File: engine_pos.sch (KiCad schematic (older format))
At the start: 12 parts, among them U5 MAX9926

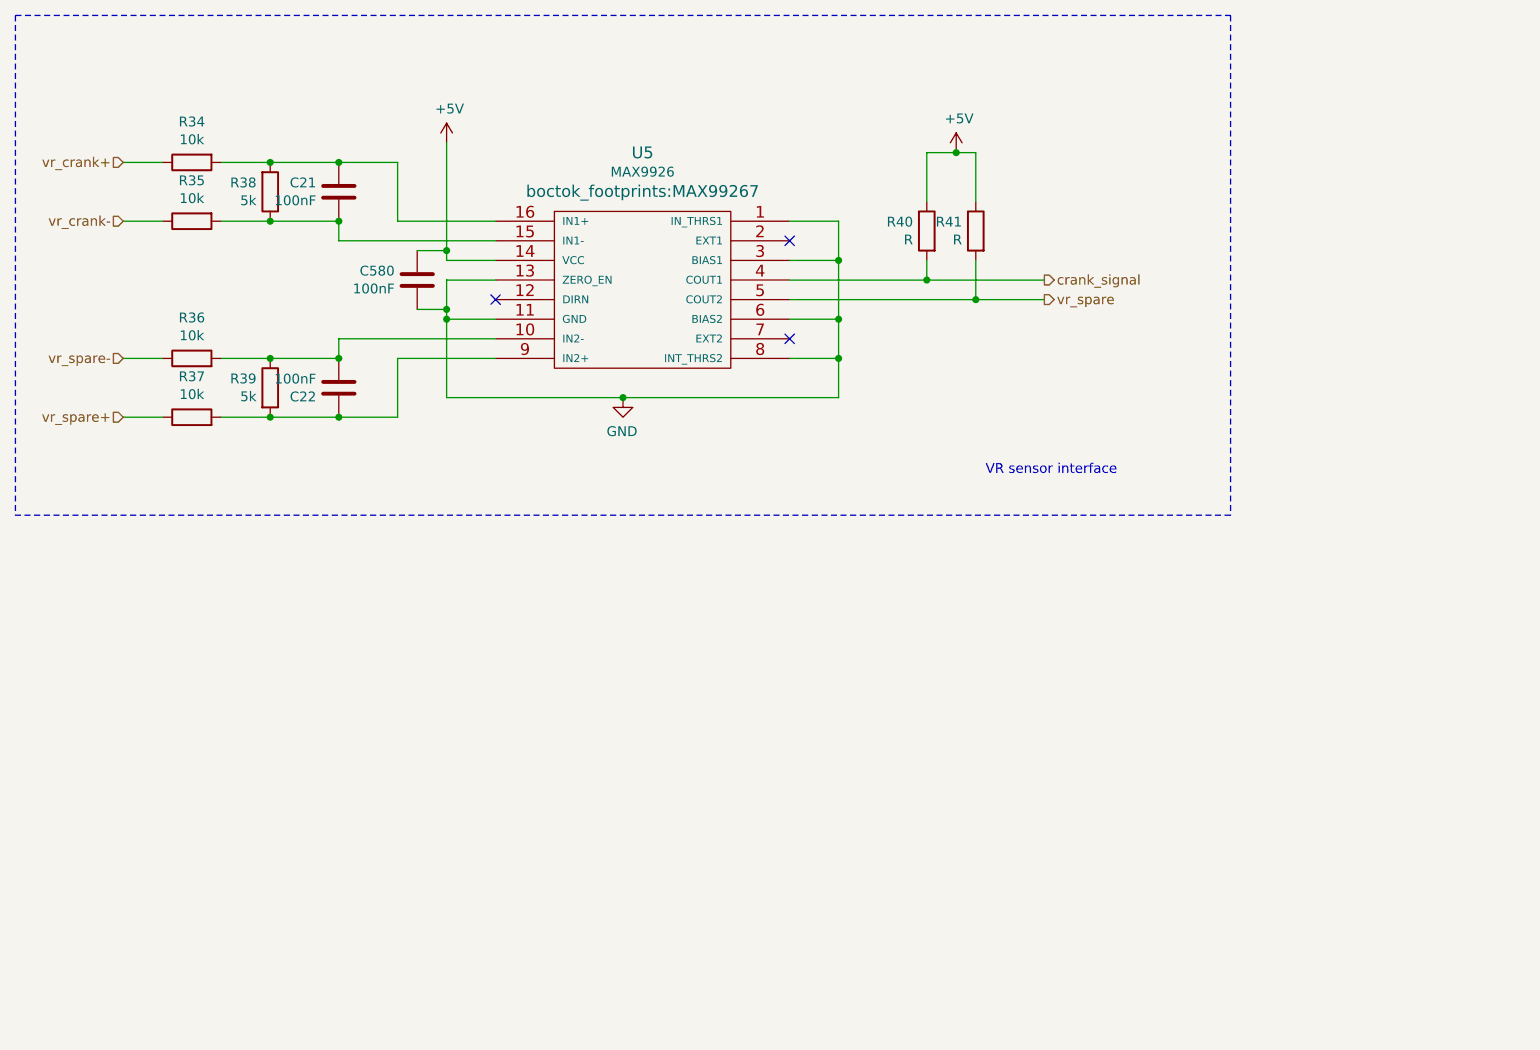
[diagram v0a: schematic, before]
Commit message: changed to discrete crank vr sensor cirquitry
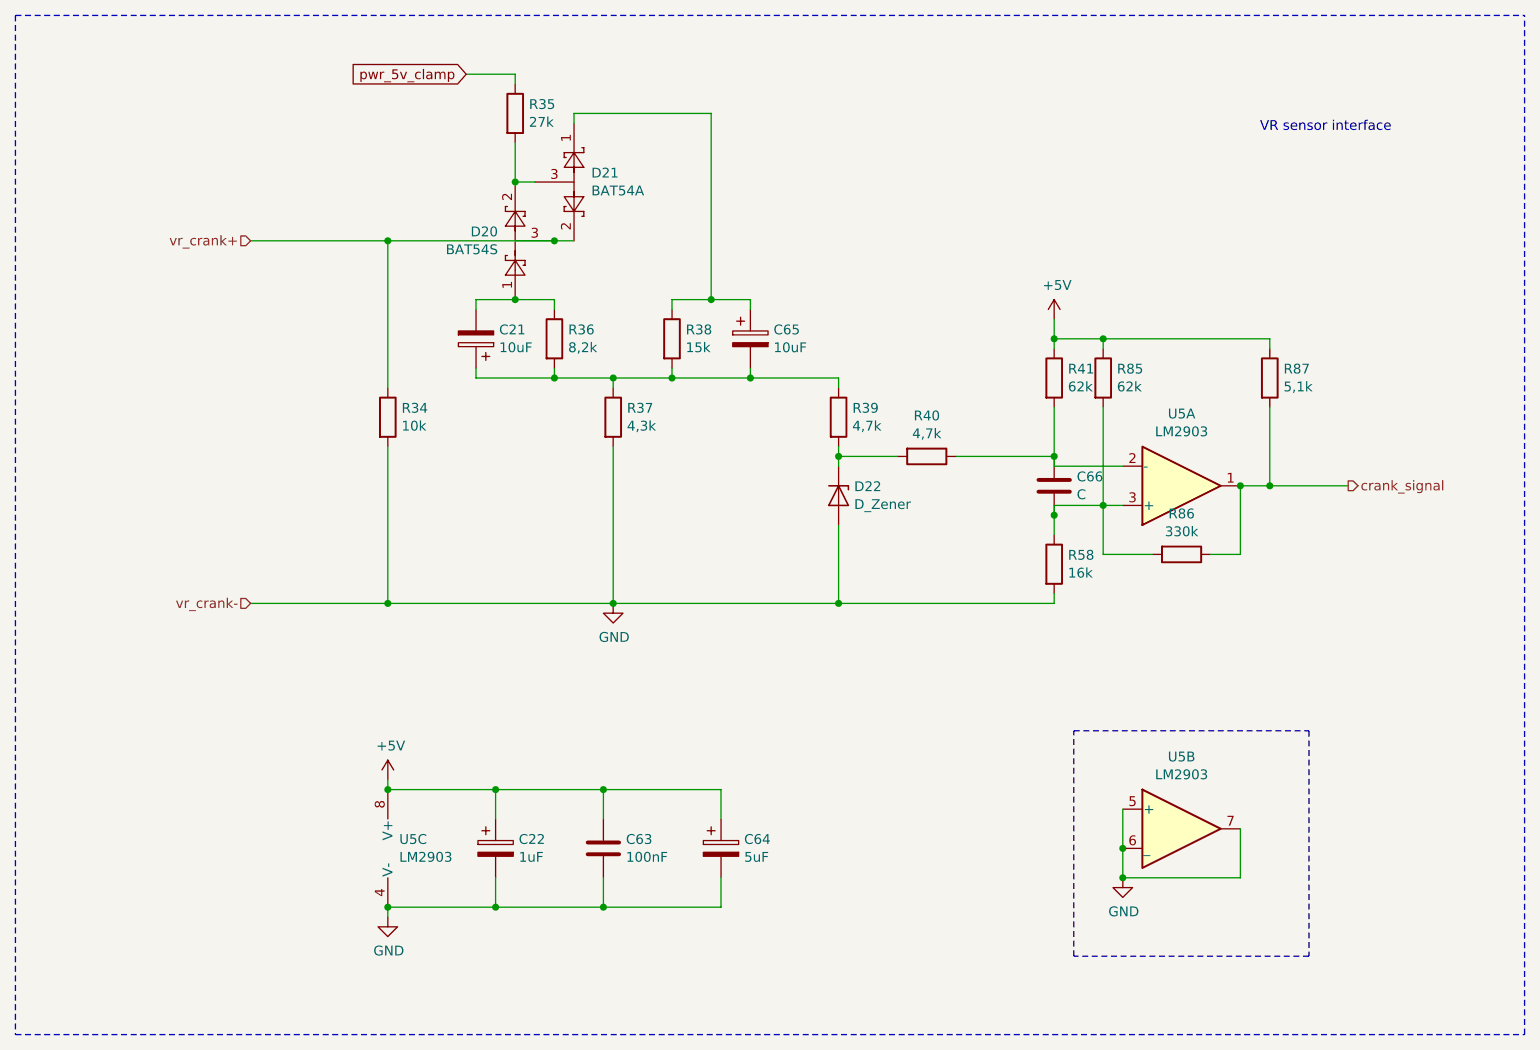
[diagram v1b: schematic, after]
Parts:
- removed C21, C22, C580: 100nF, Capacitor_SMD:C_0805_2012Metric, symbol Device:C
- removed U5: MAX9926, boctok_footprints:MAX99267, symbol boctok:MAX9926
- added C21, C65: 10uF, Capacitor_Tantalum_SMD:CP_EIA-7343-31_Kemet-D, symbol Device:CP
- added C22: 1uF, Capacitor_SMD:C_1206_3216Metric, symbol Device:CP
- added C63: 100nF, Capacitor_SMD:C_0805_2012Metric, symbol Device:C
- added C64: 5uF, Capacitor_SMD:C_1206_3216Metric, symbol Device:CP
- added C66: C, Capacitor_SMD:C_0805_2012Metric, symbol Device:C
- added D20: BAT54S, Package_TO_SOT_SMD:SOT-23, symbol boctok:BAT54S
- added D21: BAT54A, Package_TO_SOT_SMD:SOT-23, symbol boctok:BAT54A
- added D22: D_Zener, Diode_SMD:D_MiniMELF, symbol Device:D_Zener
- added R58: 16k, Resistor_SMD:R_0805_2012Metric, symbol Device:R
- added R85: 62k, Resistor_SMD:R_0805_2012Metric, symbol Device:R
- added R86: 330k, Resistor_SMD:R_0805_2012Metric, symbol Device:R
- added R87: 5,1k, Resistor_SMD:R_0805_2012Metric, symbol Device:R
- added U5: LM2903, Package_SO:SOIC-8_3.9x4.9mm_P1.27mm, symbol boctok:LM2903
- R34: footprint Resistor_SMD:R_1210_3225Metric -> Resistor_SMD:R_1206_3216Metric
- R35: value 10k -> 27k; footprint Resistor_SMD:R_1210_3225Metric -> Resistor_SMD:R_0805_2012Metric
- R36: value 10k -> 8,2k; footprint Resistor_SMD:R_1210_3225Metric -> Resistor_SMD:R_0805_2012Metric
- R37: value 10k -> 4,3k; footprint Resistor_SMD:R_1210_3225Metric -> Resistor_SMD:R_0805_2012Metric
- R38: value 5k -> 15k; footprint Resistor_SMD:R_1210_3225Metric -> Resistor_SMD:R_0805_2012Metric
- R39: value 5k -> 4,7k; footprint Resistor_SMD:R_1210_3225Metric -> Resistor_SMD:R_0805_2012Metric
- R40: value R -> 4,7k
- R41: value R -> 62k
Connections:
- net vr_spare+ is gone; now on an unnamed net: R37.1
- net +5V: now also C22.1, C63.1, C64.1, R85.1, R87.1, U5.8 (V+); no longer R40.1
- net GND: now also R34.2, R37.2, C22.2, C63.2, C64.2, D22.2 (A), R58.2, U5.4 (V-), U5.5 (+), U5.6 (_), U5.7
- net crank_signal: now also R86.1, R87.2, U5.1; no longer R40.2
- net vr_crank+: now also D20.3, D21.2
- net at R38.2: now also R36.2, R39.1, C21.1, C65.2; no longer R34.2
- net at R35.2: now also D20.2, D21.3; no longer R38.1
- net at R39.2: now also R40.2, D22.1 (K); no longer R37.2
- net vr_crank- renamed pwr_5v_clamp
- net vr_spare: no longer names the net of R41.2
- net vr_spare: now also R40.1, C66.1, U5.2 (-)
- net vr_spare-: no longer names the net of R36.1
- net vr_spare-: now also C21.2, D20.1
- new net: C65.1, D21.1, R38.1
- new net: C66.2, R58.1, R85.2, R86.2, U5.3 (+)
- no-connect marks 3 -> 0

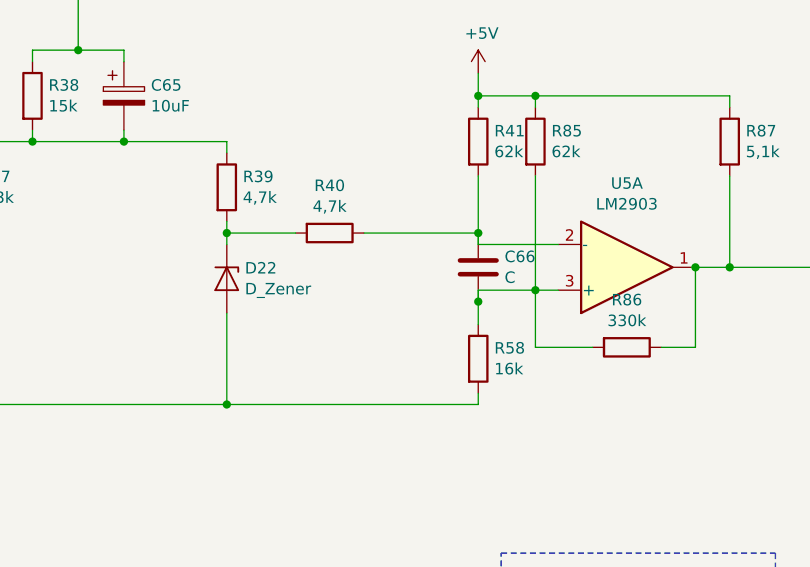
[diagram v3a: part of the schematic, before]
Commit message: added missing component values working on BOM
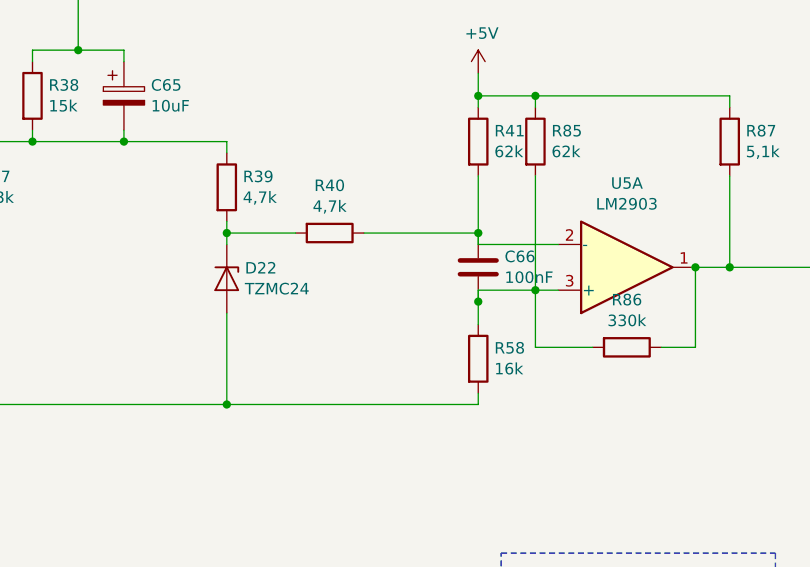
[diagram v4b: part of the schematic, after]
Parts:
- C22: Mouser (none) -> 80-C1206C105M4R
- C63: Mouser (none) -> 80-C0805C104Z3V
- C66: value C -> 100nF; Mouser (none) -> 80-C0805C104Z3V
- D20: Mouser (none) -> 863-BAT54SLT1G
- D22: value D_Zener -> TZMC24
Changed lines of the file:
@@
 F 2 "Package_TO_SOT_SMD:SOT-23" H 3575 2175 50  0001 L CNN
 F 3 "https://www.diodes.com/assets/Datasheets/ds11005.pdf" H 3380 2050 50  0001 C CNN
+F 4 "863-BAT54SLT1G" H 3500 2050 50  0001 C CNN "Mouser"
 	1    3500 2050
 	0    -1   -1   0
@@
 P 5150 3350
 F 0 "D22" V 5104 3429 50  0000 L CNN
-F 1 "D_Zener" V 5195 3429 50  0000 L CNN
+F 1 "TZMC24" V 5195 3429 50  0000 L CNN
 F 2 "Diode_SMD:D_MiniMELF" H 5150 3350 50  0001 C CNN
 F 3 "~" H 5150 3350 50  0001 C CNN
@@
 P 6250 3300
 F 0 "C66" H 6365 3346 50  0000 L CNN
-F 1 "C" H 6365 3255 50  0000 L CNN
+F 1 "100nF" H 6365 3255 50  0000 L CNN
 F 2 "Capacitor_SMD:C_0805_2012Metric" H 6288 3150 50  0001 C CNN
 F 3 "~" H 6250 3300 50  0001 C CNN
+F 4 "80-C0805C104Z3V " H 6250 3300 50  0001 C CNN "Mouser"
 	1    6250 3300
 	1    0    0    -1
@@
 F 2 "Capacitor_SMD:C_0805_2012Metric" H 3988 5000 50  0001 C CNN
 F 3 "~" H 3950 5150 50  0001 C CNN
+F 4 "80-C0805C104Z3V " H 3950 5150 50  0001 C CNN "Mouser"
 	1    3950 5150
 	1    0    0    -1
@@
 F 2 "Capacitor_SMD:C_1206_3216Metric" H 3438 5000 50  0001 C CNN
 F 3 "~" H 3400 5150 50  0001 C CNN
+F 4 "80-C1206C105M4R " H 3400 5150 50  0001 C CNN "Mouser"
 	1    3400 5150
 	1    0    0    -1

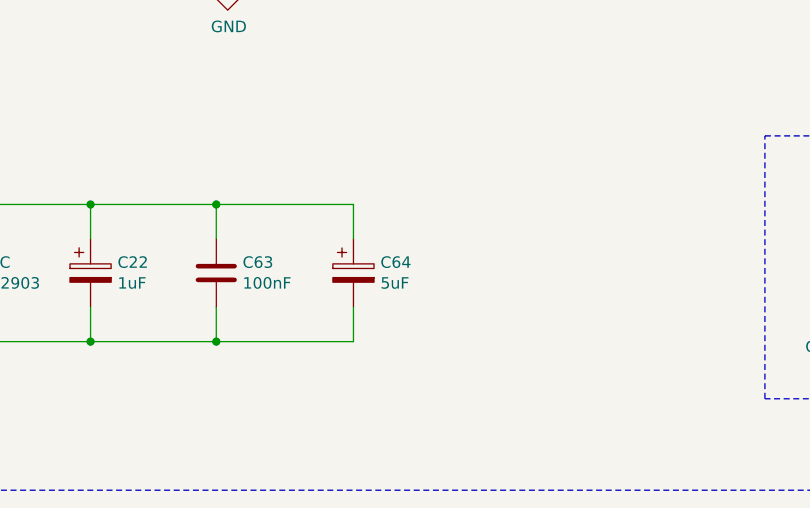
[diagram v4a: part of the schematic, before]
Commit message: cleaned BOMs
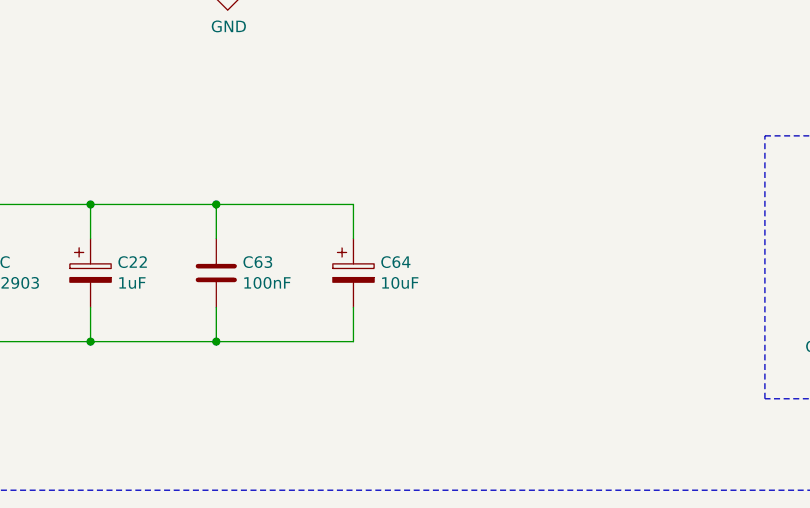
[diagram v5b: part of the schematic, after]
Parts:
- C21, C65: Mouser (none) -> 80-T491D106M035
- C64: value 5uF -> 10uF; Mouser (none) -> 80-C1206C106K4RAUTO
- D21: Mouser (none) -> 583-BAT54A
- D22: Mouser (none) -> 78-TZMC24
- R34: Mouser (none) -> 71-CRCW120610K0FKEAC
- R35: Mouser (none) -> 279-CRGCQ0805F27K
- R36: Mouser (none) -> 279-CRGCQ0805F8K2
- R37: Mouser (none) -> 71-CRCW08054K30FKEA
- R38: Mouser (none) -> 71-CRCW080515K0FKEAC
- R39, R40: Mouser (none) -> 71-CRCW08054K70FKEAC
- R41, R85: Mouser (none) -> 71-CRCW080562K0FKEA
- R58: Mouser (none) -> 71-CRCW080516K0FKEA
- R86: Mouser (none) -> 279-CRGCQ0805F330K
- R87: Mouser (none) -> 71-CRCW08055K10FKEAC
- U5: Mouser (none) -> 511-LM2903DT
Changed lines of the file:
@@
 F 2 "Resistor_SMD:R_1206_3216Metric" V 2780 2950 50  0001 C CNN
 F 3 "~" H 2850 2950 50  0001 C CNN
+F 4 "71-CRCW120610K0FKEAC " H 2850 2950 50  0001 C CNN "Mouser"
 	1    2850 2950
 	1    0    0    -1
@@
 F 2 "Resistor_SMD:R_0805_2012Metric" V 4230 2550 50  0001 C CNN
 F 3 "~" H 4300 2550 50  0001 C CNN
+F 4 "71-CRCW080515K0FKEAC" H 4300 2550 50  0001 C CNN "Mouser"
 	1    4300 2550
 	1    0    0    -1
@@
 F 2 "Capacitor_Tantalum_SMD:CP_EIA-7343-31_Kemet-D" H 4738 2400 50  0001 C CNN
 F 3 "~" H 4700 2550 50  0001 C CNN
+F 4 "80-T491D106M035" H 4700 2550 50  0001 C CNN "Mouser"
 	1    4700 2550
 	1    0    0    -1
@@
 F 2 "Resistor_SMD:R_0805_2012Metric" V 3930 2950 50  0001 C CNN
 F 3 "~" H 4000 2950 50  0001 C CNN
+F 4 "71-CRCW08054K30FKEA" H 4000 2950 50  0001 C CNN "Mouser"
 	1    4000 2950
 	1    0    0    -1
@@
 F 2 "Resistor_SMD:R_0805_2012Metric" V 5080 2950 50  0001 C CNN
 F 3 "~" H 5150 2950 50  0001 C CNN
+F 4 "71-CRCW08054K70FKEAC " H 5150 2950 50  0001 C CNN "Mouser"
 	1    5150 2950
 	1    0    0    -1
@@
 F 2 "Capacitor_Tantalum_SMD:CP_EIA-7343-31_Kemet-D" H 3338 2400 50  0001 C CNN
 F 3 "~" H 3300 2550 50  0001 C CNN
+F 4 "80-T491D106M035" H 3300 2550 50  0001 C CNN "Mouser"
 	1    3300 2550
 	-1   0    0    1
@@
 F 2 "Resistor_SMD:R_0805_2012Metric" V 3630 2550 50  0001 C CNN
 F 3 "~" H 3700 2550 50  0001 C CNN
+F 4 "279-CRGCQ0805F8K2" H 3700 2550 50  0001 C CNN "Mouser"
 	1    3700 2550
 	1    0    0    -1
@@
 F 2 "Package_TO_SOT_SMD:SOT-23" H 3875 1875 50  0001 L CNN
 F 3 "http://www.diodes.com/_files/datasheets/ds11005.pdf" H 3680 1750 50  0001 C CNN
+F 4 "583-BAT54A" H 3800 1750 50  0001 C CNN "Mouser"
 	1    3800 1750
 	0    1    1    0
@@
 F 2 "Diode_SMD:D_MiniMELF" H 5150 3350 50  0001 C CNN
 F 3 "~" H 5150 3350 50  0001 C CNN
+F 4 "78-TZMC24 " H 5150 3350 50  0001 C CNN "Mouser"
 	1    5150 3350
 	0    1    1    0
@@
 F 2 "Resistor_SMD:R_0805_2012Metric" V 3430 1400 50  0001 C CNN
 F 3 "~" H 3500 1400 50  0001 C CNN
+F 4 "279-CRGCQ0805F27K" H 3500 1400 50  0001 C CNN "Mouser"
 	1    3500 1400
 	1    0    0    -1
@@
 F 2 "Package_SO:SOIC-8_3.9x4.9mm_P1.27mm" H 6900 3300 50  0001 C CNN
 F 3 "http://www.ti.com/lit/ds/symlink/lm393-n.pdf" H 6900 3300 50  0001 C CNN
+F 4 "511-LM2903DT" H 6900 3300 50  0001 C CNN "Mouser"
 	1    6900 3300
 	1    0    0    1
@@
 F 2 "Package_SO:SOIC-8_3.9x4.9mm_P1.27mm" H 6900 5050 50  0001 C CNN
 F 3 "http://www.ti.com/lit/ds/symlink/lm393-n.pdf" H 6900 5050 50  0001 C CNN
+F 4 "511-LM2903DT" H 6900 5050 50  0001 C CNN "Mouser"
 	2    6900 5050
 	1    0    0    -1
@@
 F 2 "Package_SO:SOIC-8_3.9x4.9mm_P1.27mm" H 2950 5150 50  0001 C CNN
 F 3 "http://www.ti.com/lit/ds/symlink/lm393-n.pdf" H 2950 5150 50  0001 C CNN
+F 4 "511-LM2903DT" H 2950 5150 50  0001 C CNN "Mouser"
 	3    2950 5150
 	1    0    0    -1
@@
 F 2 "Resistor_SMD:R_0805_2012Metric" V 5530 3150 50  0001 C CNN
 F 3 "~" H 5600 3150 50  0001 C CNN
+F 4 "71-CRCW08054K70FKEAC " H 5600 3150 50  0001 C CNN "Mouser"
 	1    5600 3150
 	0    1    1    0
@@
 F 2 "Resistor_SMD:R_0805_2012Metric" V 6180 3700 50  0001 C CNN
 F 3 "~" H 6250 3700 50  0001 C CNN
+F 4 "71-CRCW080516K0FKEA" H 6250 3700 50  0001 C CNN "Mouser"
 	1    6250 3700
 	1    0    0    -1
@@
 F 2 "Resistor_SMD:R_0805_2012Metric" V 6830 3650 50  0001 C CNN
 F 3 "~" H 6900 3650 50  0001 C CNN
+F 4 "279-CRGCQ0805F330K" H 6900 3650 50  0001 C CNN "Mouser"
 	1    6900 3650
 	0    1    1    0
@@
 F 2 "Resistor_SMD:R_0805_2012Metric" V 6180 2750 50  0001 C CNN
 F 3 "~" H 6250 2750 50  0001 C CNN
+F 4 "71-CRCW080562K0FKEA" H 6250 2750 50  0001 C CNN "Mouser"
 	1    6250 2750
 	1    0    0    -1
@@
 F 2 "Resistor_SMD:R_0805_2012Metric" V 6430 2750 50  0001 C CNN
 F 3 "~" H 6500 2750 50  0001 C CNN
+F 4 "71-CRCW080562K0FKEA" H 6500 2750 50  0001 C CNN "Mouser"
 	1    6500 2750
 	1    0    0    -1
@@
 F 2 "Resistor_SMD:R_0805_2012Metric" V 7280 2750 50  0001 C CNN
 F 3 "~" H 7350 2750 50  0001 C CNN
+F 4 "71-CRCW08055K10FKEAC" H 7350 2750 50  0001 C CNN "Mouser"
 	1    7350 2750
 	1    0    0    -1
@@
 P 4550 5150
 F 0 "C64" H 4668 5196 50  0000 L CNN
-F 1 "5uF" H 4668 5105 50  0000 L CNN
+F 1 "10uF" H 4668 5105 50  0000 L CNN
 F 2 "Capacitor_SMD:C_1206_3216Metric" H 4588 5000 50  0001 C CNN
 F 3 "~" H 4550 5150 50  0001 C CNN
+F 4 "80-C1206C106K4RAUTO " H 4550 5150 50  0001 C CNN "Mouser"
 	1    4550 5150
 	1    0    0    -1
